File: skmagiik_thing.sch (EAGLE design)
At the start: 24 parts, among them J1 MAGJACK-NOLABELS, U1 AUDIO-JACK, U2 AUDIO-JACK, U3 MAX3232

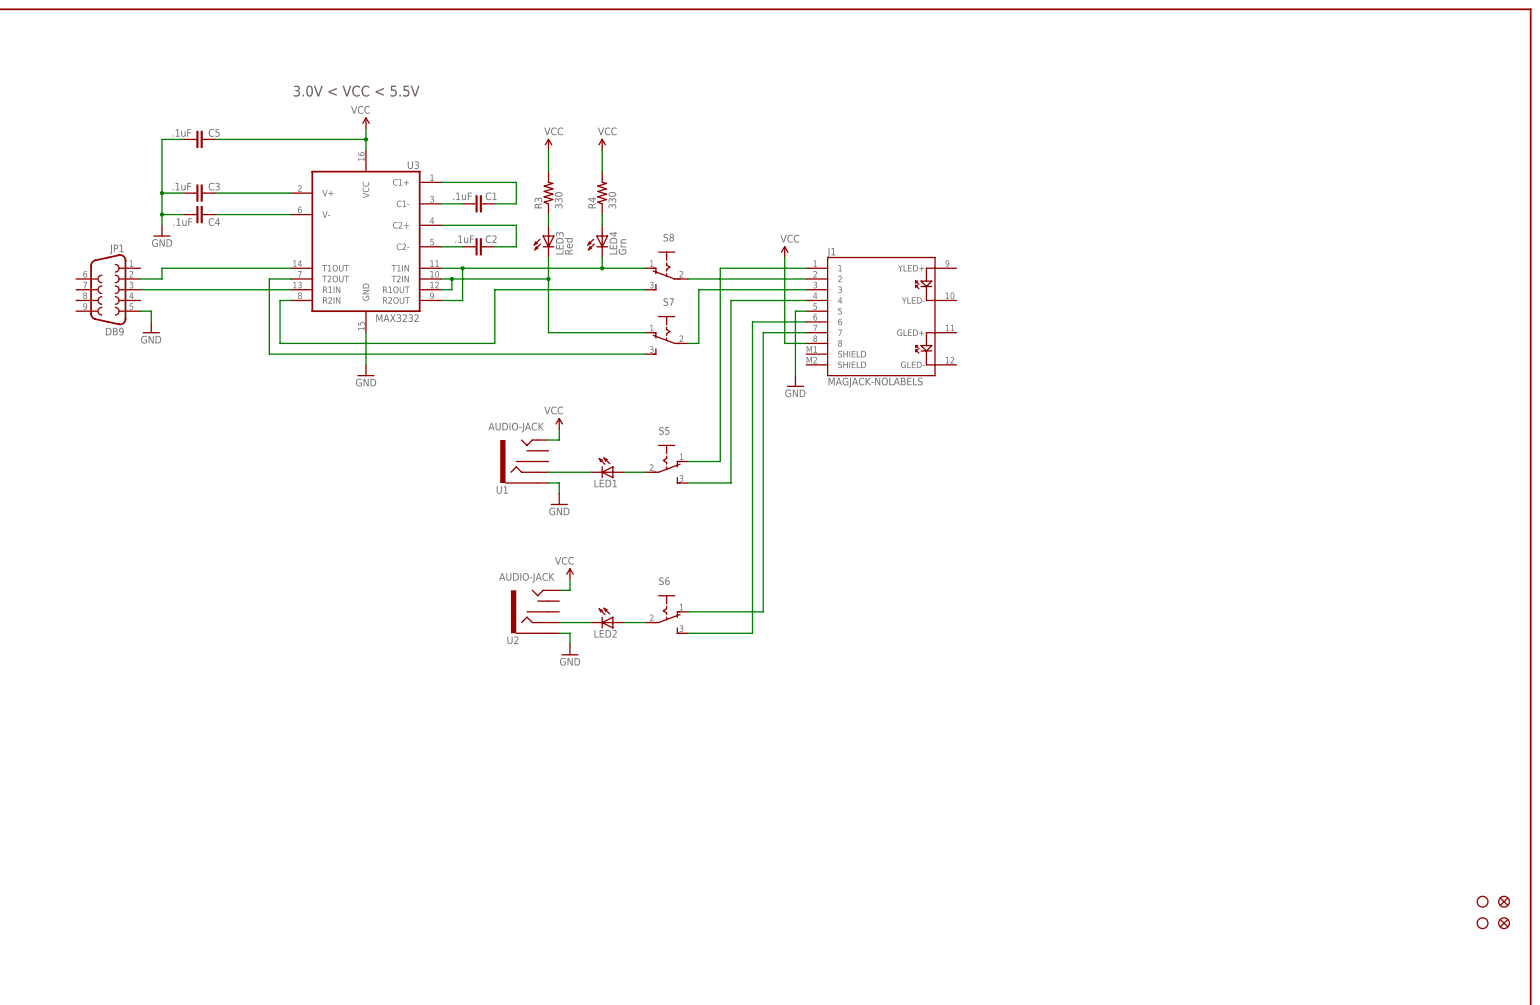
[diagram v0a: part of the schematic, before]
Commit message: changed to use modules, added pdf of layout
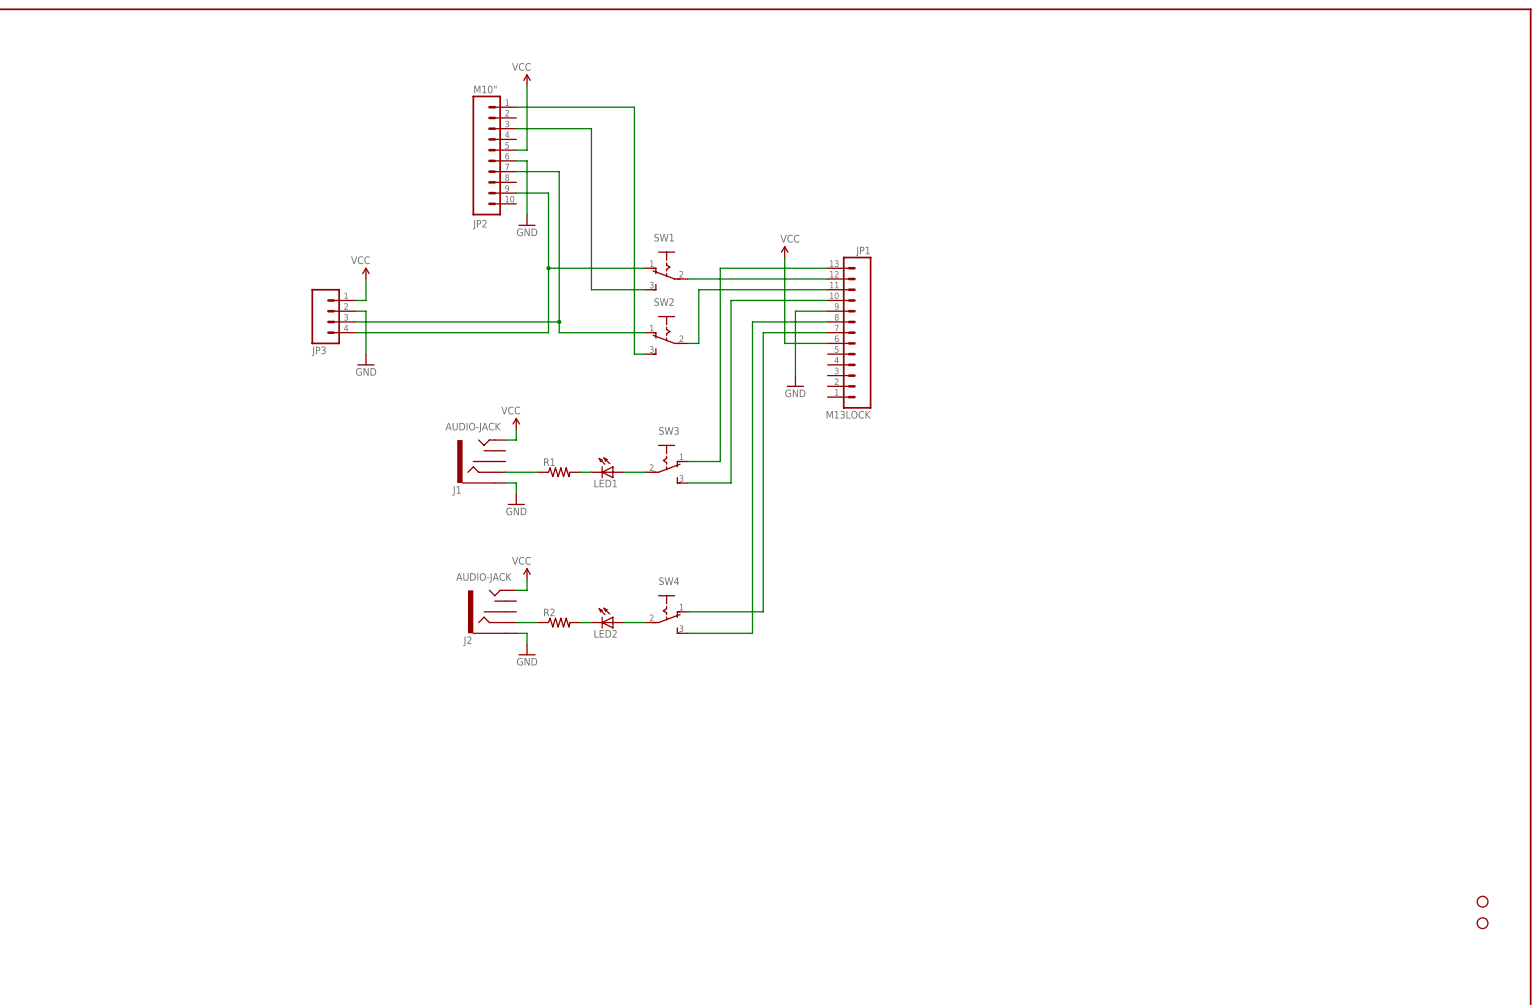
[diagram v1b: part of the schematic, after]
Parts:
- removed C1, C2, C3, C4, C5: .1uF, SparkFun-Capacitors:0.1UF-25V(+80/-20%)(0603)
- removed FID1, FID2: FIDUCIAL1X2, SparkFun-Aesthetics:FIDUCIAL1X2
- removed LED3: Red, SparkFun:LED1206
- removed LED4: Grn, SparkFun:LED1206
- removed R3, R4: 330, SparkFun:RESISTOR0603-RES
- removed U1, U2: AUDIO-JACK, SparkFun:AUDIO-JACK2PTH
- removed U3: MAX3232, SparkFun-DigitalIC:MAX232SOIC16
- added J2: AUDIO-JACK, SparkFun:AUDIO-JACK2PTH
- added JP2: M10", SparkFun-Connectors:M10"
- added JP3: (no value), SparkFun:M04PTH
- added R1, R2: (no value), resistor:R-US_0207/10
- J1: value MAGJACK-NOLABELS -> AUDIO-JACK; device SparkFun-Connectors:MAGJACK-NOLABELS -> SparkFun:AUDIO-JACK2PTH
- JP1: value DB9 -> M13LOCK; device Testing:DB9L17SM209S114T -> SparkFun-Connectors:M13LOCK
- renumbered S5 to SW3, S6 to SW4, S7 to SW2, S8 to SW1
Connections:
- removed net C1+: C1.1, U3.C1+
- removed net C1-: C1.2, U3.C1-
- removed net C2+: C2.1, U3.C2+
- removed net C2-: C2.2, U3.C2-
- removed net N$15: SW1.S, U3.R2IN
- removed net N$16: SW2.S, U3.T2OUT
- removed net V+: C3.1, U3.V+
- removed net V-: C4.1, U3.V-
- net GND: now also J1.SLEEVE, J2.SLEEVE, JP1.9, JP2.6, JP3.2; no longer C3.2, C4.2, C5.2, J1.5, JP1.5, U1.SLEEVE, U2.SLEEVE, U3.GND
- net N$1: now also J2.RING, R2.1; no longer LED2.C, U2.RING
- net N$10: now also JP2.1, SW2.S; no longer LED4.A, R4.1
- net N$11: now also JP2.9, JP3.4, SW1.O; no longer JP1.3, U3.R1IN
- net N$12: now also LED1.C, R1.2; no longer JP1.2, U3.T1OUT
- net N$13: now also JP2.3, SW1.S; no longer LED4.C, SW1.O, U3.R2OUT, U3.T1IN
- net N$14: now also LED2.C, R2.2; no longer LED3.C, SW2.O, U3.R1OUT, U3.T2IN
- net N$17: now also JP1.12; no longer J1.2
- net N$18: now also JP1.11; no longer J1.3
- net N$2: now also J1.RING, R1.1; no longer LED1.C, U1.RING
- net N$3: now also JP1.7; no longer J1.7
- net N$4: now also JP1.8; no longer J1.6
- net N$5: now also JP1.10; no longer J1.4
- net N$6: now also JP1.13; no longer J1.1
- net N$9: now also JP2.7, JP3.3, SW2.O; no longer LED3.A, R3.1
- net VCC: now also J1.TIP, J2.TIP, JP1.6, JP2.5, JP3.1; no longer C5.1, J1.8, R3.2, R4.2, U1.TIP, U2.TIP, U3.VCC
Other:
- note removed: "3.0V < VCC < 5.5V"

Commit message: layour ready for aproval
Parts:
- removed JP1: M13LOCK, SparkFun-Connectors:M13LOCK
- added J3: RJ45, pjb:RJ45
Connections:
- net GND: now also J3.5; no longer JP1.9
- net N$17: now also J3.2; no longer JP1.12
- net N$18: now also J3.3; no longer JP1.11
- net N$3: now also J3.7; no longer JP1.7
- net N$4: now also J3.6; no longer JP1.8
- net N$5: now also J3.4; no longer JP1.10
- net N$6: now also J3.1; no longer JP1.13
- net VCC: now also J3.8; no longer JP1.6
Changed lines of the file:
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@@
 <part name="STANDOFF3" library="SparkFun-Electromechanical" deviceset="STAND-OFF" device=""/>
 <part name="STANDOFF5" library="SparkFun-Electromechanical" deviceset="STAND-OFF" device=""/>
-<part name="JP1" library="SparkFun-Connectors" deviceset="M13" device="LOCK" value="M13LOCK"/>
 <part name="JP2" library="SparkFun-Connectors" deviceset="M10" device="&quot;">
 <attribute name="NO_PART" value="1"/>
@@
 <part name="R1" library="resistor" deviceset="R-US_" device="0207/10"/>
 <part name="R2" library="resistor" deviceset="R-US_" device="0207/10"/>
+<part name="J3" library="pjb" deviceset="RJ45" device=""/>
 </parts>
 <sheets>
@@
 <instance part="STANDOFF3" gate="G$1" x="388.62" y="55.88"/>
 <instance part="STANDOFF5" gate="G$1" x="388.62" y="50.8"/>
-<instance part="JP1" gate="G$1" x="243.84" y="190.5" rot="MR0"/>
 <instance part="JP2" gate="G$1" x="149.86" y="226.06" rot="MR180">
 <attribute name="NO_PART" x="149.86" y="226.06" size="3.81" layer="96" rot="MR180" display="off"/>
@@
 <instance part="R1" gate="G$1" x="170.18" y="157.48"/>
 <instance part="R2" gate="G$1" x="170.18" y="121.92"/>
+<instance part="J3" gate="G$1" x="236.22" y="198.12"/>
 </instances>
 <busses>
@@
 <pinref part="GND6" gate="1" pin="GND"/>
 <wire x1="226.06" y1="195.58" x2="226.06" y2="180.34" width="0.1524" layer="91"/>
-<pinref part="JP1" gate="G$1" pin="9"/>
-<wire x1="226.06" y1="195.58" x2="233.68" y2="195.58" width="0.1524" layer="91"/>
+<wire x1="226.06" y1="195.58" x2="231.14" y2="195.58" width="0.1524" layer="91"/>
+<pinref part="J3" gate="G$1" pin="5"/>
 </segment>
 <segment>
@@
 <pinref part="P+5" gate="1" pin="VCC"/>
 <wire x1="223.52" y1="208.28" x2="223.52" y2="187.96" width="0.1524" layer="91"/>
-<pinref part="JP1" gate="G$1" pin="6"/>
-<wire x1="223.52" y1="187.96" x2="233.68" y2="187.96" width="0.1524" layer="91"/>
+<wire x1="223.52" y1="187.96" x2="231.14" y2="187.96" width="0.1524" layer="91"/>
+<pinref part="J3" gate="G$1" pin="8"/>
 </segment>
 <segment>
@@
 <net name="N$3" class="0">
 <segment>
-<wire x1="233.68" y1="190.5" x2="218.44" y2="190.5" width="0.1524" layer="91"/>
+<wire x1="231.14" y1="190.5" x2="218.44" y2="190.5" width="0.1524" layer="91"/>
 <wire x1="218.44" y1="190.5" x2="218.44" y2="124.46" width="0.1524" layer="91"/>
 <pinref part="SW4" gate="1" pin="O"/>
 <wire x1="200.66" y1="124.46" x2="218.44" y2="124.46" width="0.1524" layer="91"/>
-<pinref part="JP1" gate="G$1" pin="7"/>
+<pinref part="J3" gate="G$1" pin="7"/>
 </segment>
 </net>
@@
 <wire x1="200.66" y1="119.38" x2="215.9" y2="119.38" width="0.1524" layer="91"/>
 <wire x1="215.9" y1="119.38" x2="215.9" y2="193.04" width="0.1524" layer="91"/>
-<wire x1="215.9" y1="193.04" x2="233.68" y2="193.04" width="0.1524" layer="91"/>
-<pinref part="JP1" gate="G$1" pin="8"/>
+<wire x1="215.9" y1="193.04" x2="231.14" y2="193.04" width="0.1524" layer="91"/>
+<pinref part="J3" gate="G$1" pin="6"/>
 </segment>
 </net>
 <net name="N$5" class="0">
 <segment>
-<wire x1="233.68" y1="198.12" x2="210.82" y2="198.12" width="0.1524" layer="91"/>
+<wire x1="231.14" y1="198.12" x2="210.82" y2="198.12" width="0.1524" layer="91"/>
 <wire x1="210.82" y1="198.12" x2="210.82" y2="154.94" width="0.1524" layer="91"/>
 <pinref part="SW3" gate="1" pin="S"/>
 <wire x1="210.82" y1="154.94" x2="200.66" y2="154.94" width="0.1524" layer="91"/>
-<pinref part="JP1" gate="G$1" pin="10"/>
+<pinref part="J3" gate="G$1" pin="4"/>
 </segment>
 </net>
@@
 <wire x1="200.66" y1="160.02" x2="208.28" y2="160.02" width="0.1524" layer="91"/>
 <wire x1="208.28" y1="160.02" x2="208.28" y2="205.74" width="0.1524" layer="91"/>
-<wire x1="208.28" y1="205.74" x2="233.68" y2="205.74" width="0.1524" layer="91"/>
-<pinref part="JP1" gate="G$1" pin="13"/>
+<wire x1="208.28" y1="205.74" x2="231.14" y2="205.74" width="0.1524" layer="91"/>
+<pinref part="J3" gate="G$1" pin="1"/>
 </segment>
 </net>
@@
 <net name="N$17" class="0">
 <segment>
-<wire x1="233.68" y1="203.2" x2="200.66" y2="203.2" width="0.1524" layer="91"/>
+<wire x1="231.14" y1="203.2" x2="200.66" y2="203.2" width="0.1524" layer="91"/>
 <pinref part="SW1" gate="1" pin="P"/>
-<pinref part="JP1" gate="G$1" pin="12"/>
+<pinref part="J3" gate="G$1" pin="2"/>
 </segment>
 </net>
 <net name="N$18" class="0">
 <segment>
-<wire x1="233.68" y1="200.66" x2="203.2" y2="200.66" width="0.1524" layer="91"/>
+<wire x1="231.14" y1="200.66" x2="203.2" y2="200.66" width="0.1524" layer="91"/>
 <wire x1="203.2" y1="200.66" x2="203.2" y2="187.96" width="0.1524" layer="91"/>
 <pinref part="SW2" gate="1" pin="P"/>
 <wire x1="203.2" y1="187.96" x2="200.66" y2="187.96" width="0.1524" layer="91"/>
-<pinref part="JP1" gate="G$1" pin="11"/>
-</segment>
-</net>
+<pinref part="J3" gate="G$1" pin="3"/>
+</segment>
+</net>

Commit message: exported gerbers
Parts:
- added U$2: PROJECT_LOGO, links_misc:PROJECT_LOGO
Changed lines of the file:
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@@
 <part name="R2" library="resistor" deviceset="R-US_" device="0207/10"/>
 <part name="J3" library="pjb" deviceset="RJ45" device=""/>
+<part name="U$2" library="links_misc" deviceset="PROJECT_LOGO" device=""/>
 </parts>
 <sheets>
@@
 <instance part="R2" gate="G$1" x="170.18" y="121.92"/>
 <instance part="J3" gate="G$1" x="236.22" y="198.12"/>
+<instance part="U$2" gate="G$1" x="314.96" y="53.34"/>
 </instances>
 <busses>
